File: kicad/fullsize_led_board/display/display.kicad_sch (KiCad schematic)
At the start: 772 parts, among them J1 Anodes Header, J2 Stabilizer Header (Top), J3 Cathodes Header, J4 Stabilizer Header (Left)

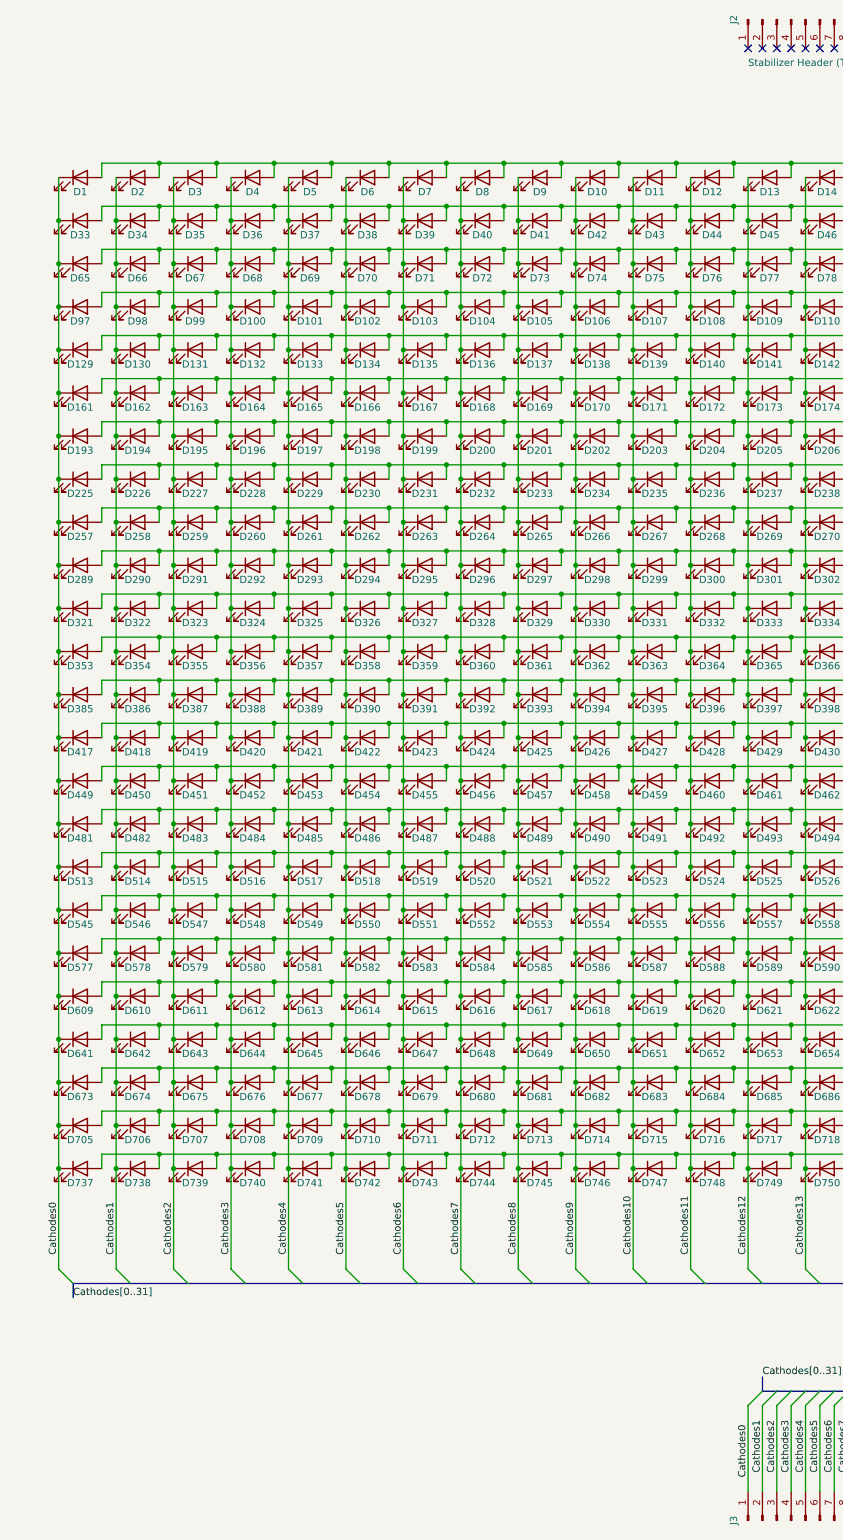
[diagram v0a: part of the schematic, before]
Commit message: fullsize led board: started pcb layout of the display
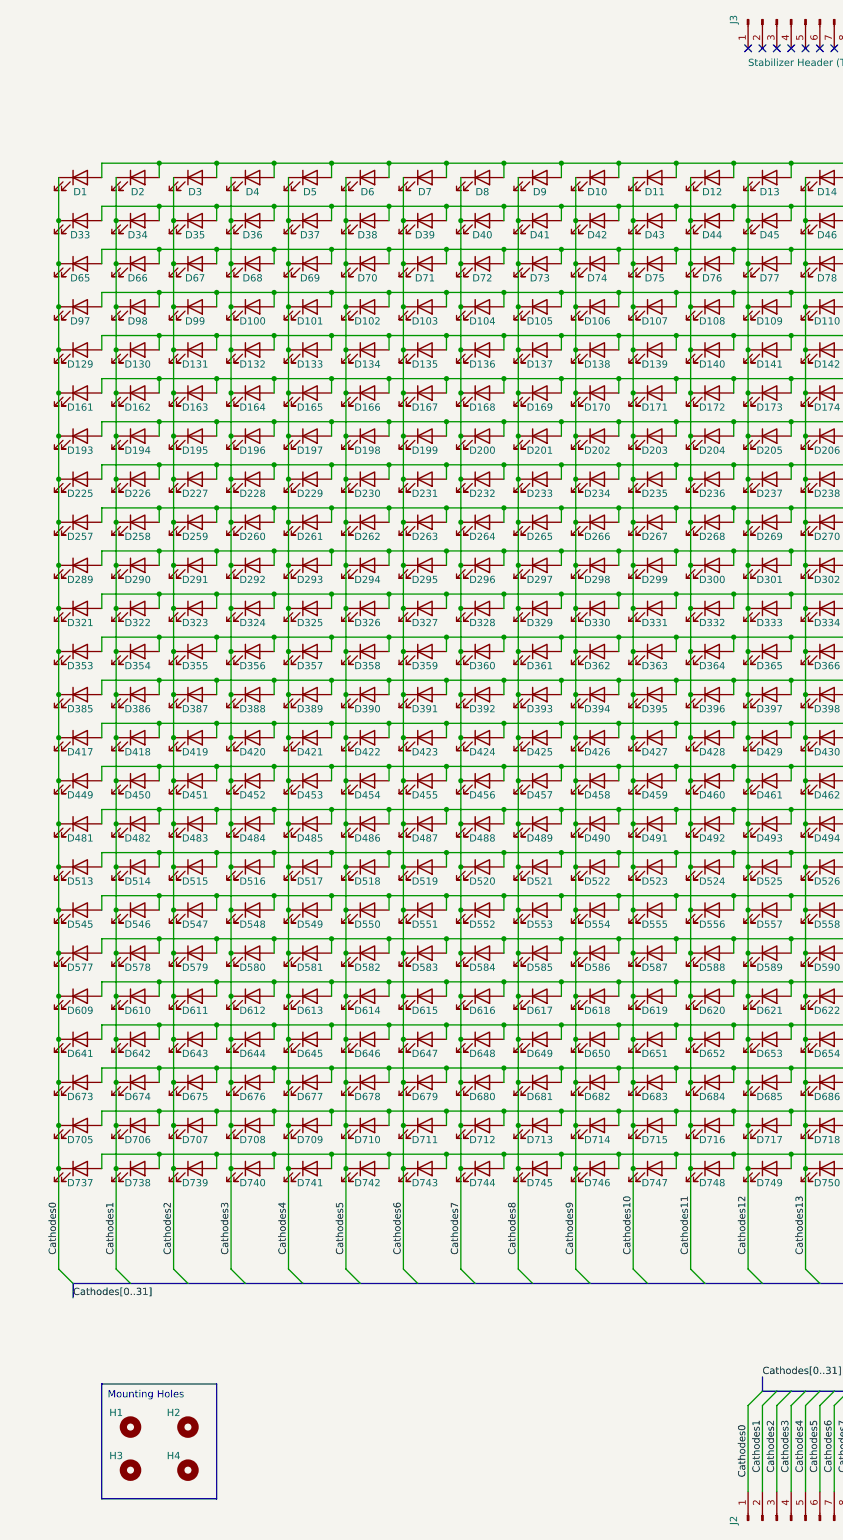
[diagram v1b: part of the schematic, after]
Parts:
- added H1, H2, H3, H4: ~, MountingHole:MountingHole_3mm, symbol Mechanical:MountingHole
- renumbered J3 to J2, J2 to J3

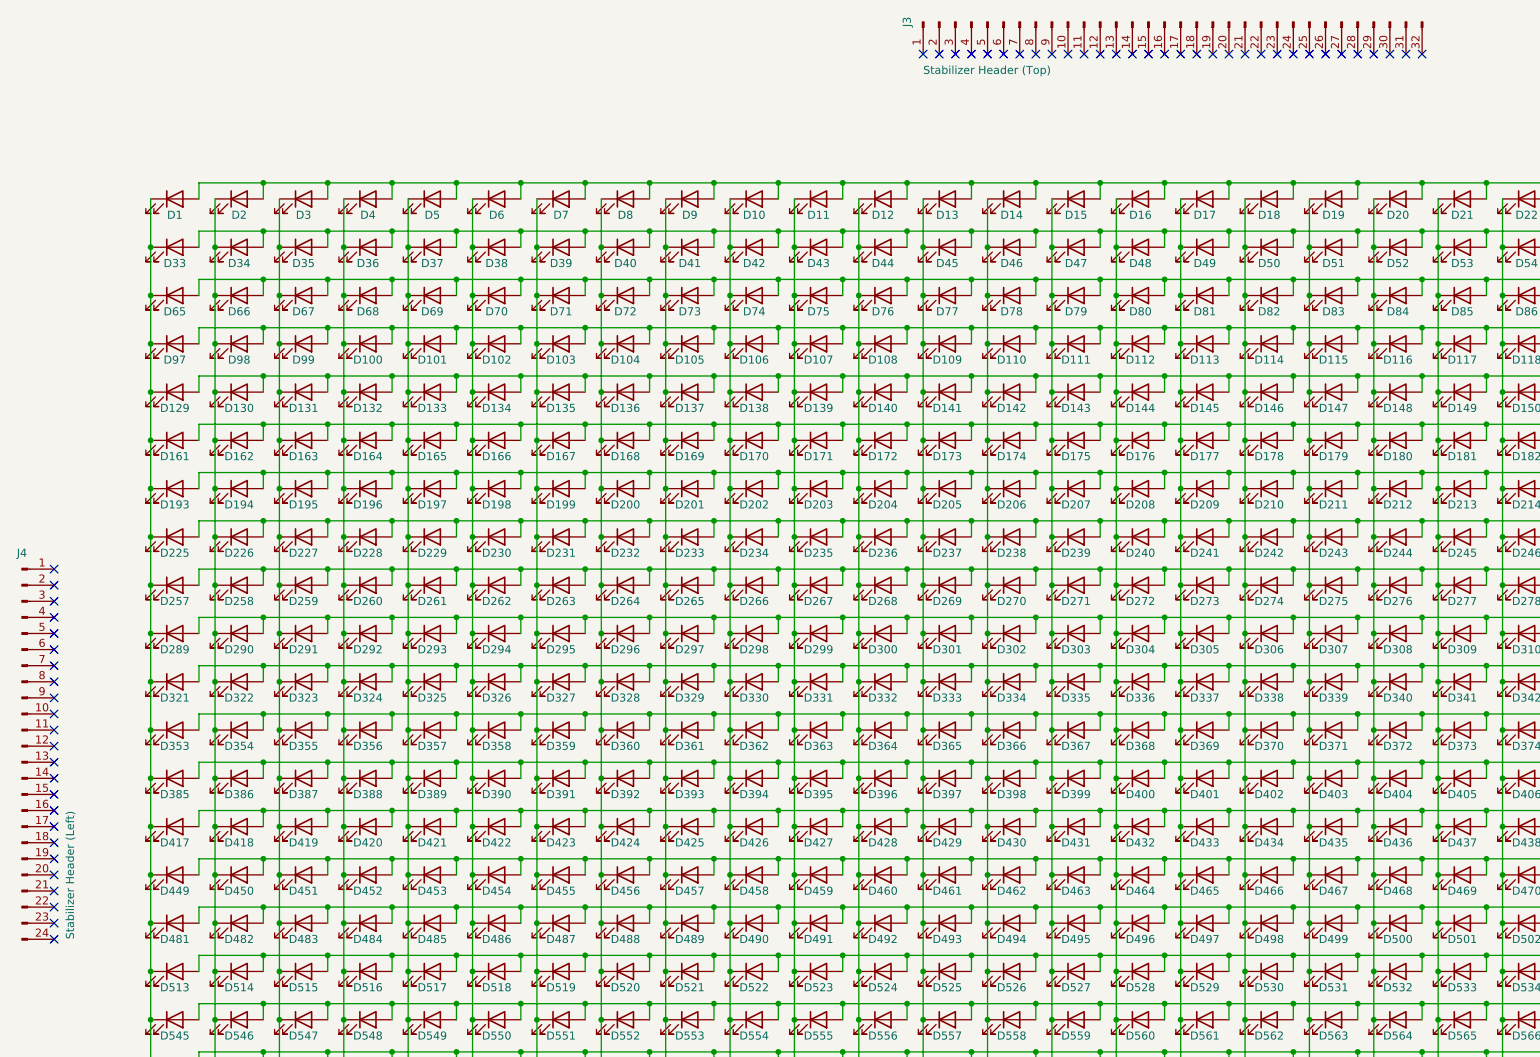
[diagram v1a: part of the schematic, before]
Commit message: fullsize led board: display pcb wired
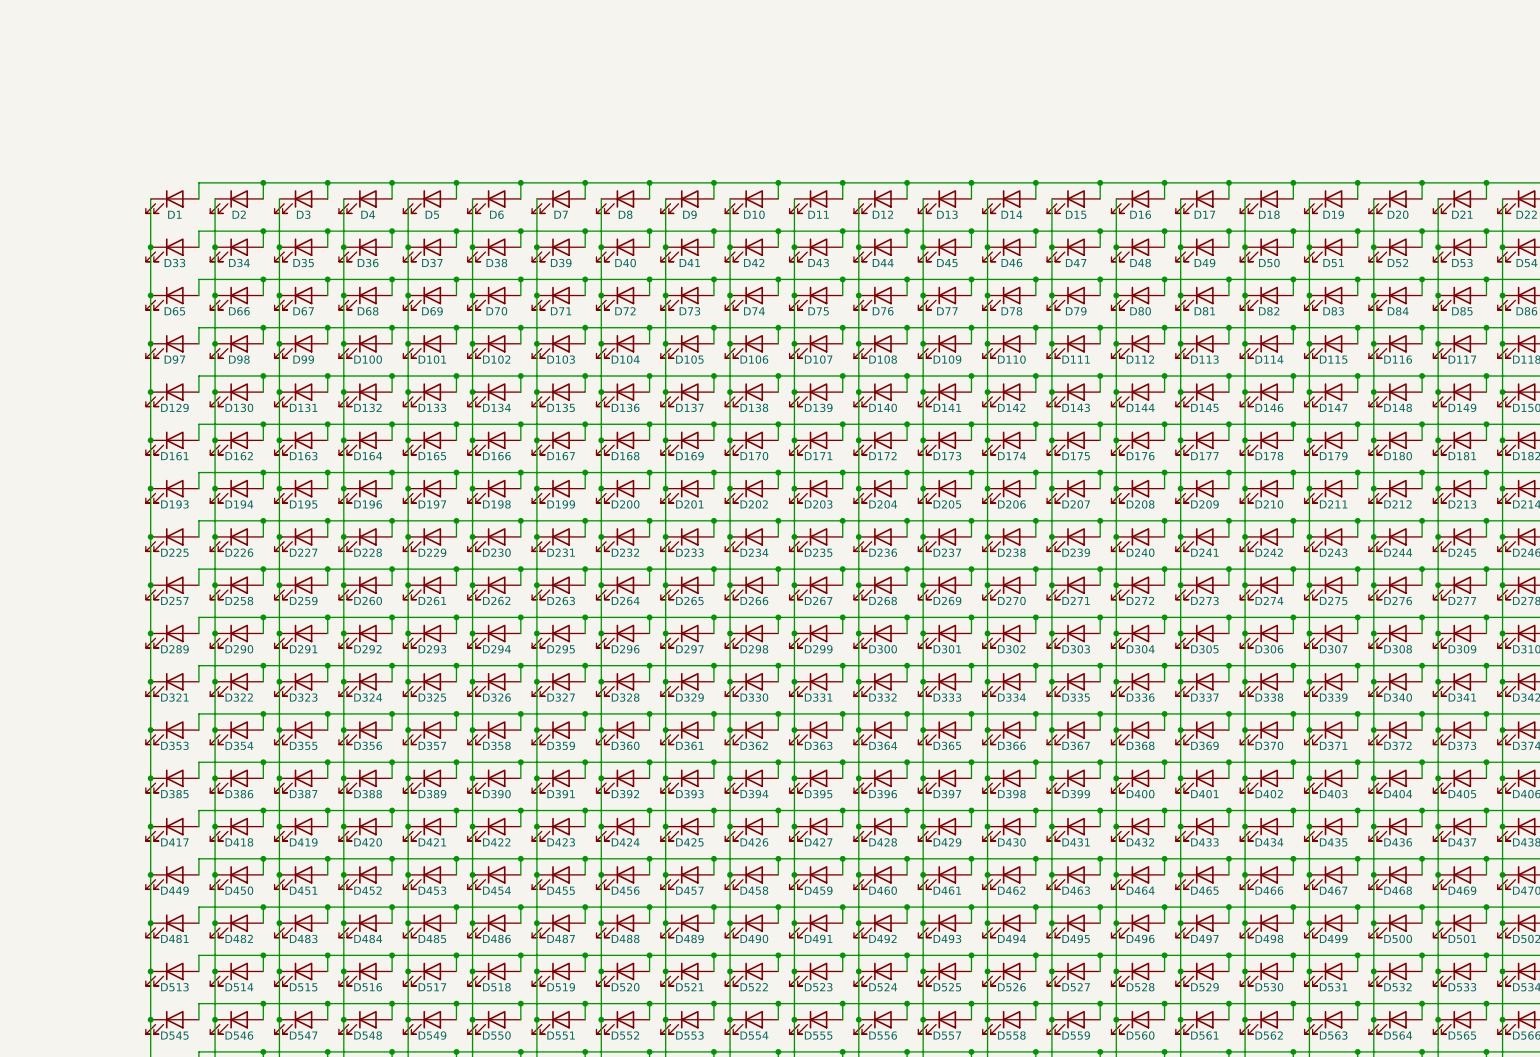
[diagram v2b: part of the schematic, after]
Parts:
- removed J3: Stabilizer Header (Top), Connector_PinHeader_2.54mm:PinHeader_1x32_P2.54mm_Vertical, symbol Connector:Conn_01x32_Pin
- removed J4: Stabilizer Header (Left), Connector_PinHeader_2.54mm:PinHeader_1x24_P2.54mm_Vertical, symbol Connector:Conn_01x24_Pin
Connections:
- no-connect marks 56 -> 0
